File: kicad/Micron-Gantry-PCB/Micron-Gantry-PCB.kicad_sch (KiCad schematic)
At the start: 70 parts, among them J1 CAN_IN, J10 USB_C_Receptacle_USB2.0, J2 CAN_OUT, J3 M0_THERM, J4 M1_THERM, J5 Conn_01x04_Male, J6 Conn_01x04_Male, J7 ENDSTOP1, J8 ENDSTOP2, SW1 SW_Push, U1 TMC2209-LA-T, U2 STM32G0B1CEU6, U3 TMC2209-LA-T, U4 TCAN334, U5 NCP730BMT330TBG, Y1 Crystal_GND24

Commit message: Work in progress, layout close to finish
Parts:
- H1, H2: footprint MountingHole:MountingHole_3.2mm_M3_DIN965 -> Project:MountingHole_3.2mm_M3
- gave numbers to parts that had none: 2
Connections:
- net CHAM_THERM: now also U2.12 (PA1); no longer U2.24 (PB12)
- net ENDSTOP1: now also U2.14 (PA3); no longer U2.12 (PA1)
- net GND: now also J3.1 (Pin_1), J4.1 (Pin_1); no longer J3.2 (Pin_2), J4.2 (Pin_2)
- net M0_DIR: now also U2.20 (PB1); no longer U2.21 (PB2)
- net M0_STEP: now also U2.21 (PB2); no longer U2.20 (PB1)
- net M0_THERM: now also U2.23 (PB11); no longer U2.22 (PB10)
- net M0_UART: now also U2.15 (PA4); no longer U2.13 (PA2)
- net M0_UART_RX: now also U2.16 (PA5); no longer U2.14 (PA3)
- net M1_DIAG: now also U2.44 (PB5); no longer U2.47 (PB8)
- net M1_DIR: now also U2.47 (PB8); no longer U2.46 (PB7)
- net M1_STEP: now also U2.46 (PB7); no longer U2.45 (PB6)
- net M1_THERM: now also U2.24 (PB12); no longer U2.23 (PB11)
- net at R11.2, R12.2: now also J4.2 (Pin_2); no longer J4.1 (Pin_1)
- net at R5.2, R6.2: now also J3.2 (Pin_2); no longer J3.1 (Pin_1)
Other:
- note added: "Motor A/B statt 0/1"
- note added: "Umbennnen"

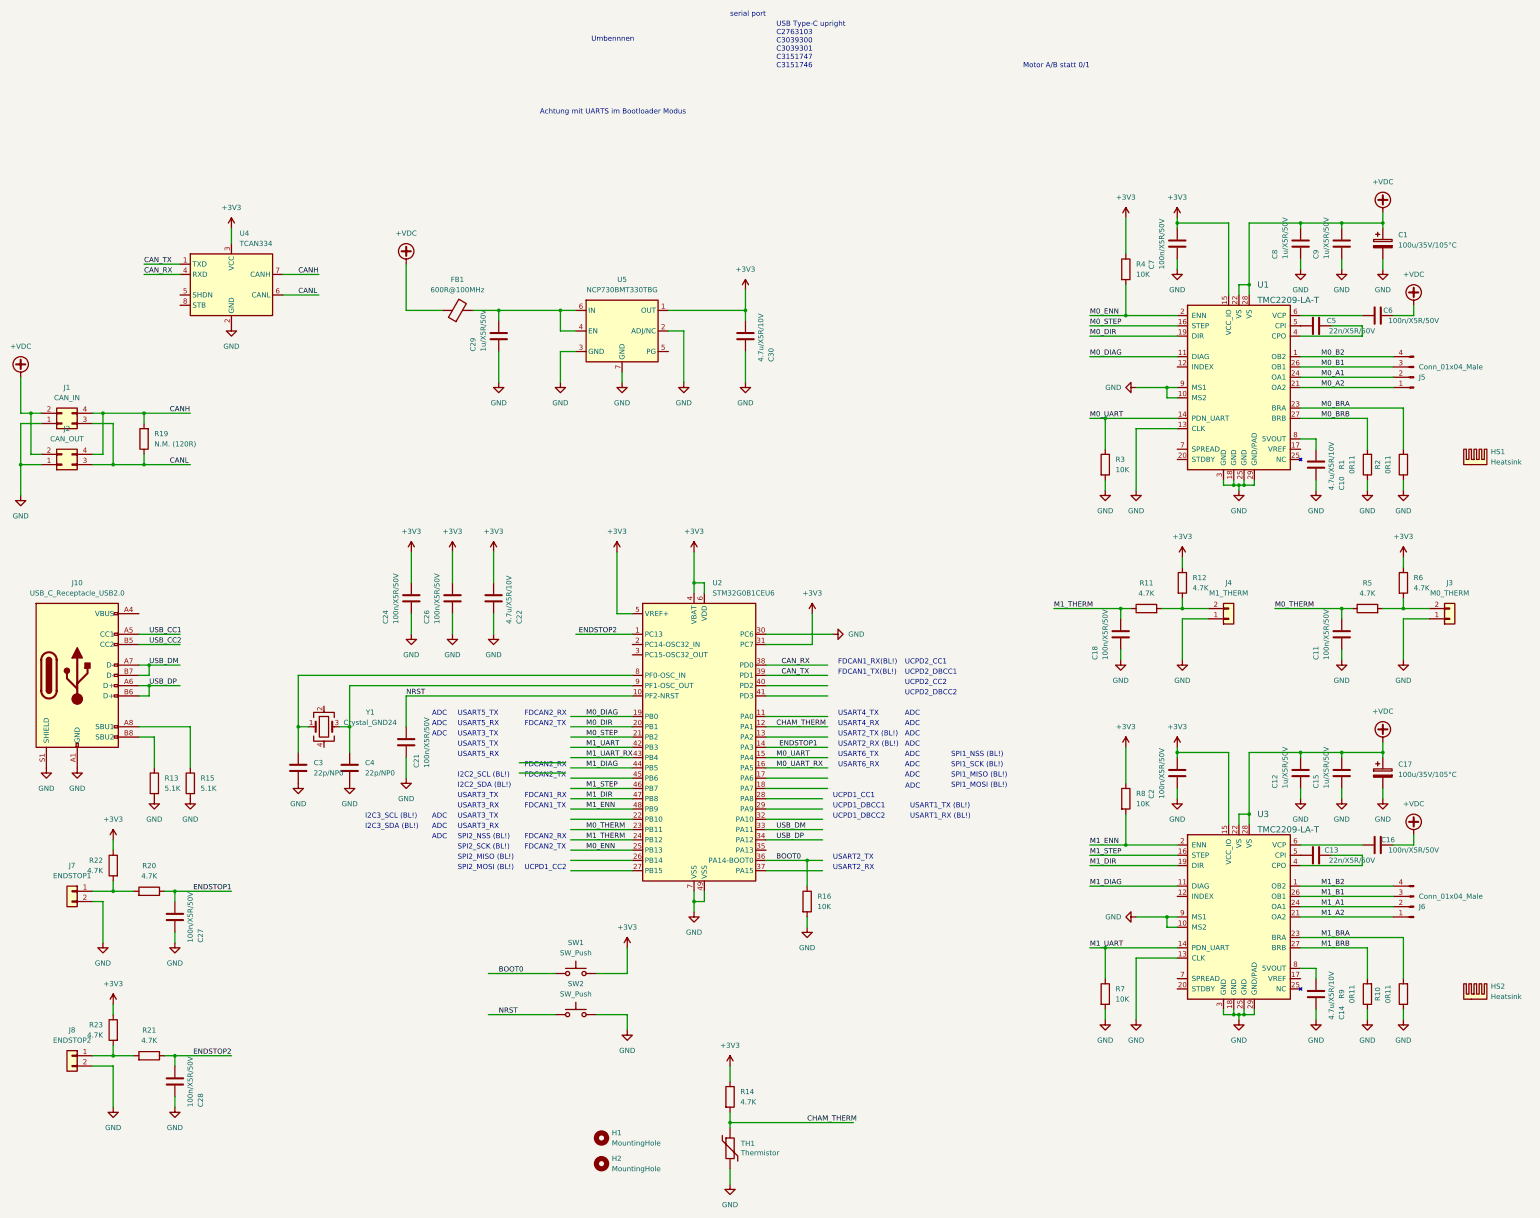
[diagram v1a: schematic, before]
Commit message: Corrected USB footprint, renamed some signals
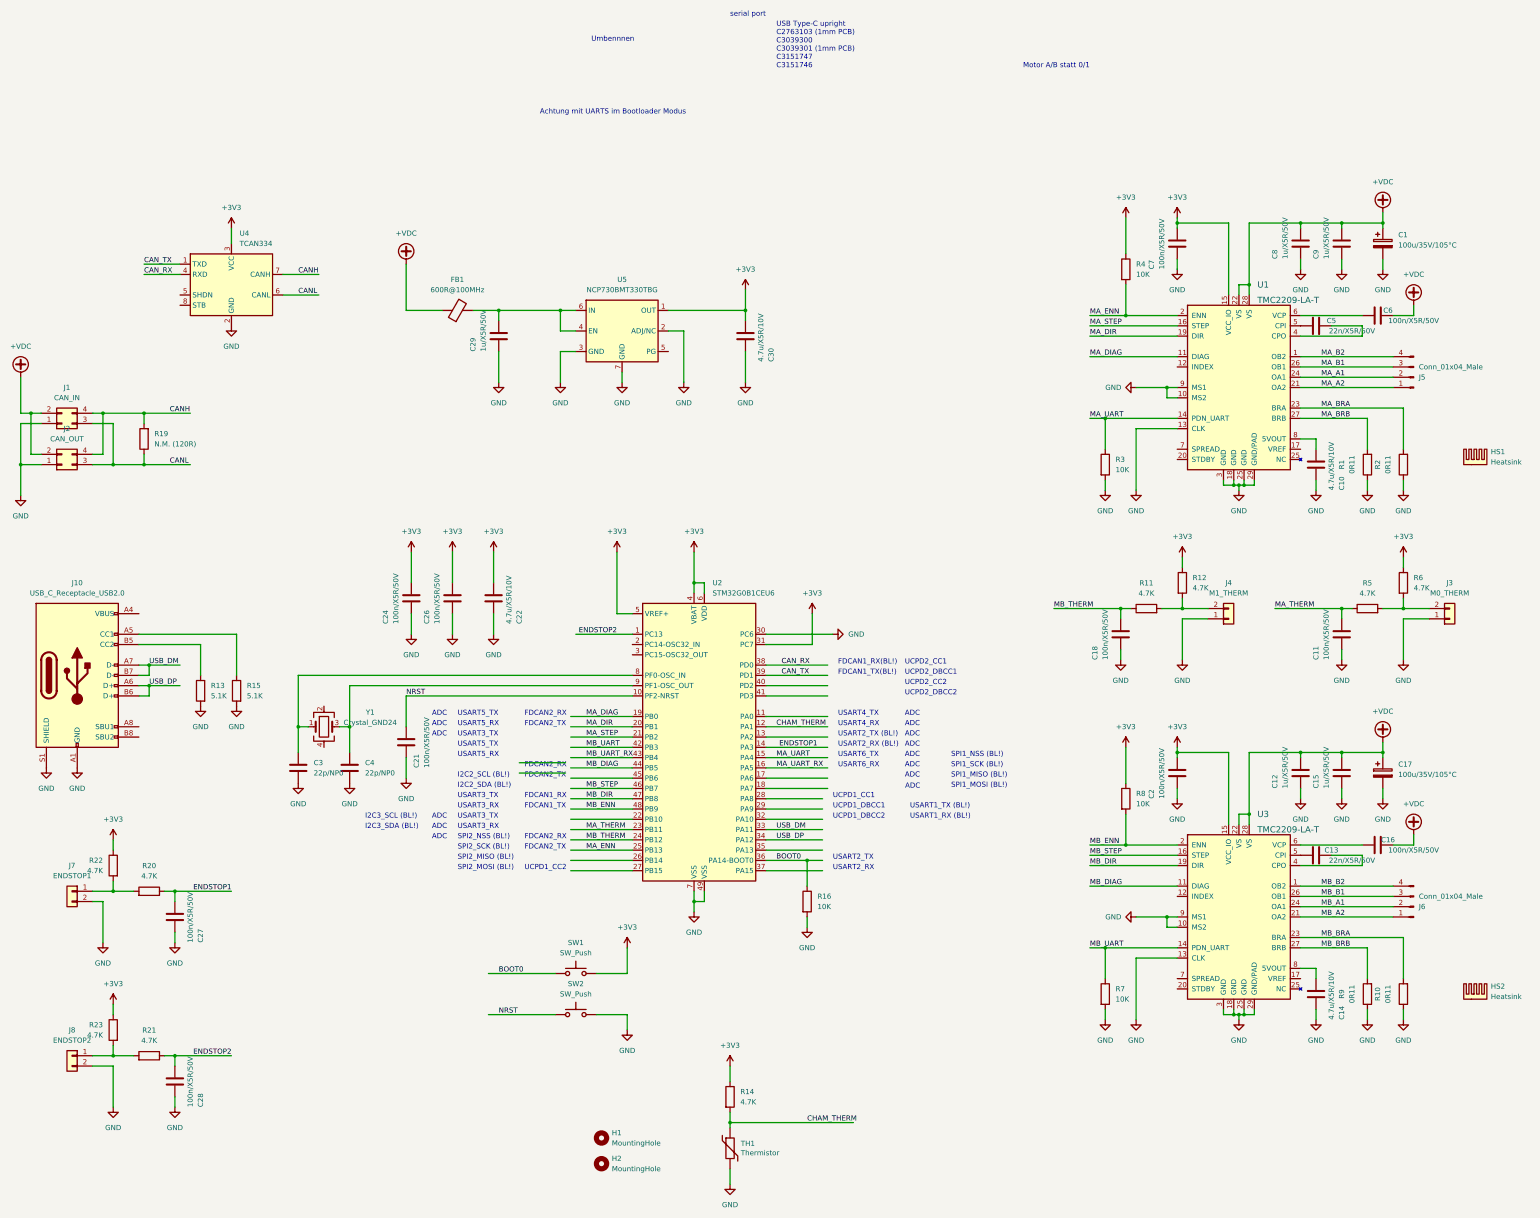
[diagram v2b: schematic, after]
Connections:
- net USB_CC1 is gone; now on an unnamed net: J10.A5 (CC1)
- net USB_CC2 is gone; now on an unnamed net: J10.B5 (CC2)
- net at R15.1: no longer J10.A8 (SBU1)
- net at R13.1: no longer J10.B8 (SBU2)
- net M0_A1 renamed MA_A1
- net M0_A2 renamed MA_A2
- net M0_B1 renamed MA_B1
- net M0_B2 renamed MA_B2
- net M0_BRA renamed MA_BRA
- net M0_BRB renamed MA_BRB
- net M0_DIAG renamed MA_DIAG
- net M0_DIR renamed MA_DIR
- net M0_ENN renamed MA_ENN
- net M0_STEP renamed MA_STEP
- net M0_THERM renamed MA_THERM
- net M0_UART renamed MA_UART
- net M0_UART_RX renamed MA_UART_RX
- net M1_A1 renamed MB_A1
- net M1_A2 renamed MB_A2
- net M1_B1 renamed MB_B1
- net M1_B2 renamed MB_B2
- net M1_BRA renamed MB_BRA
- net M1_BRB renamed MB_BRB
- net M1_DIAG renamed MB_DIAG
- net M1_DIR renamed MB_DIR
- net M1_ENN renamed MB_ENN
- net M1_STEP renamed MB_STEP
- net M1_THERM renamed MB_THERM
- net M1_UART renamed MB_UART
- net M1_UART_RX renamed MB_UART_RX
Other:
- note added: "USB Type-C upright C2763103 (1mm PCB) C3039300 C3039301 (1mm PCB) C3151747 C3151746"
- note removed: "USB Type-C upright C2763103 C3039300 C3039301 C3151747 C3151746"
- moved on the sheet: R13, R15
